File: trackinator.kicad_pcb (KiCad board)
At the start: 2 copper layers, 83 x 33.1 mm, 7 parts, among them U1 ESP32-S3, U2 ESP32-S3, U3 ESP32-S3, U4 ESP32-S3, U5 ESP32-S3, U6 FE2.1

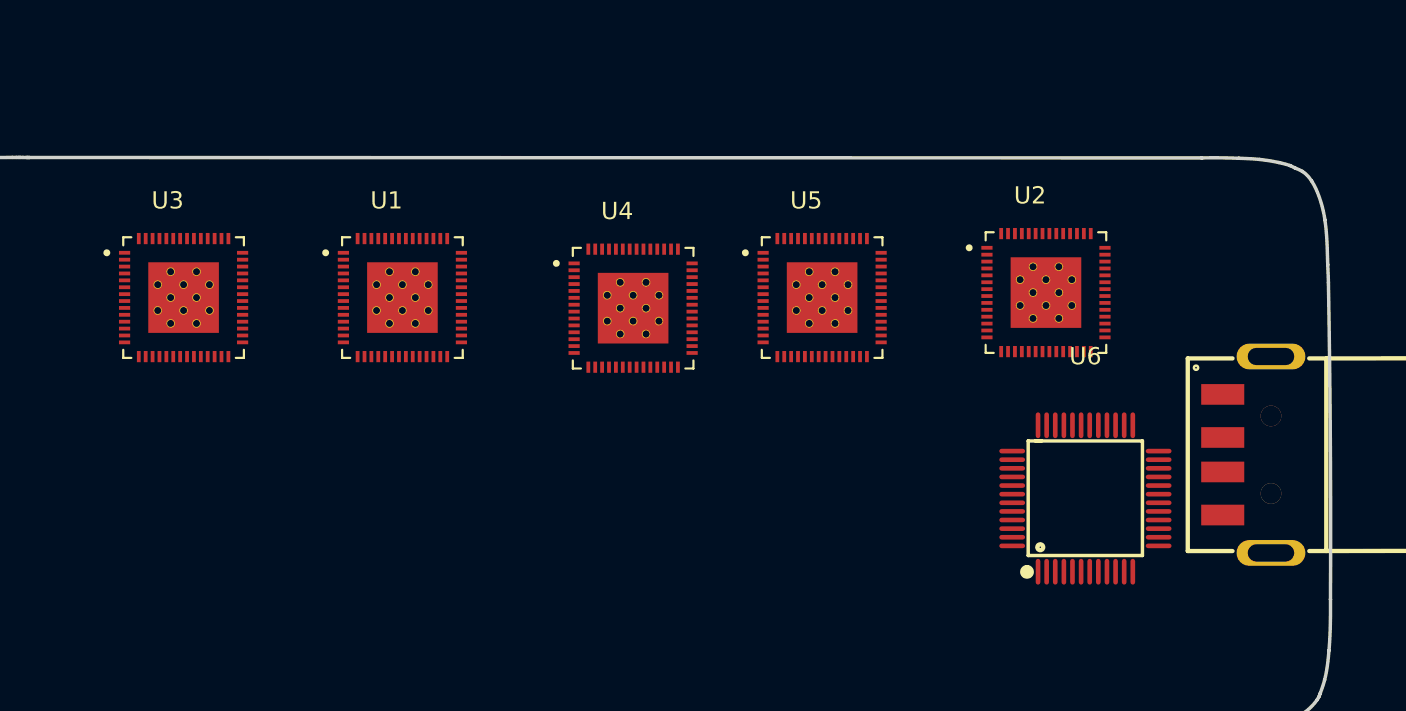
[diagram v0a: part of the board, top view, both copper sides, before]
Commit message: FFC camera connector + pin mapping
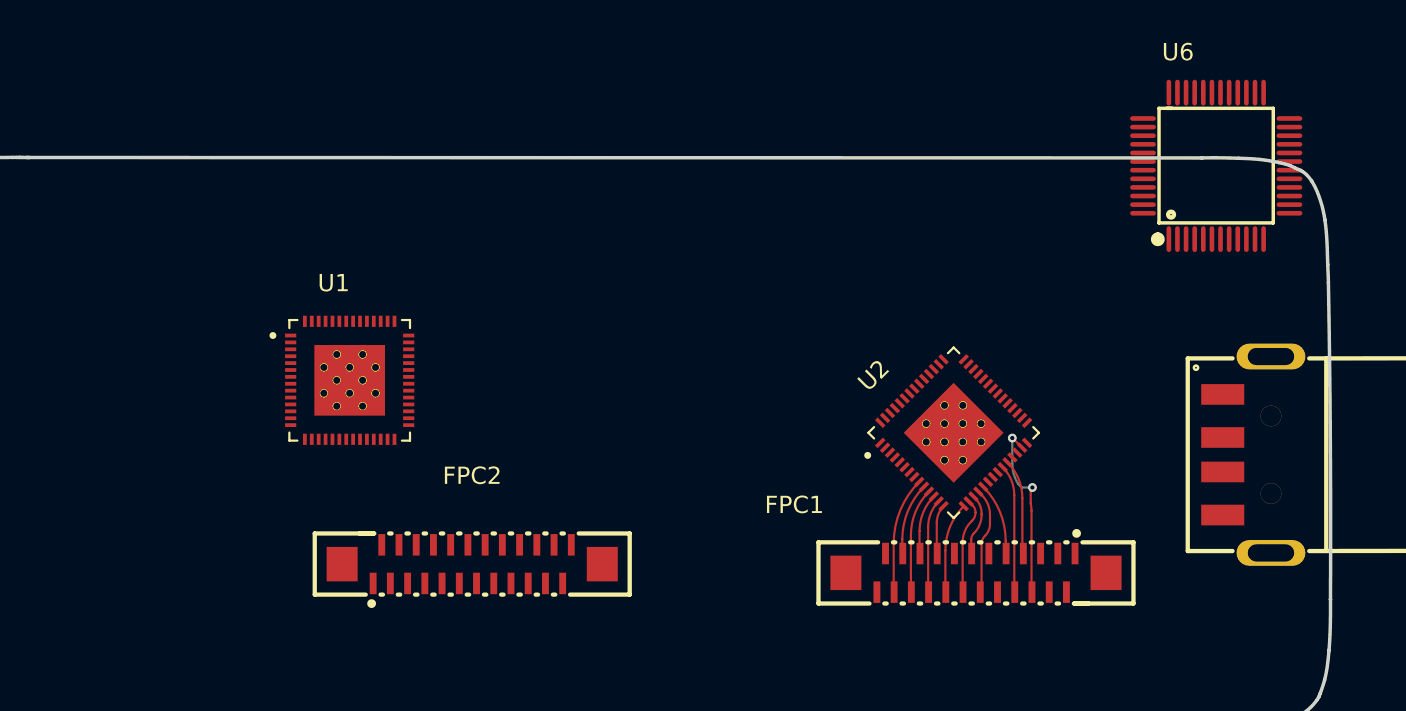
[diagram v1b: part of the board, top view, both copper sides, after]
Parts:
- removed U3, U4, U5: ESP32-S3, mylib:IC_ESP32-S3
- added FPC1: F0503-ZV-24-20T-R, easyeda2kicad:FPC-SMD_F0503-ZV-24-20T-R, F.Cu at (205.3, 57.7)
- added FPC2: F0503-ZV-24-20T-R, easyeda2kicad:FPC-SMD_F0503-ZV-24-20T-R, F.Cu at (176.0, 57.1)
- moved U6 20.7 mm to (219.2, 34.0)
- moved U2 9.74 mm to (204.0, 49.5), turned to 45 degrees
- moved U1 5.69 mm to (168.9, 46.5)
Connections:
- U1 pad 10: unconnected-(U1-GPIO5-Pad10) -> /ESP32_2/DVP_Y3
- U1 pad 11: unconnected-(U1-GPIO6-Pad11) -> /ESP32_2/DVP_Y5
- U1 pad 12: unconnected-(U1-GPIO7-Pad12) -> /ESP32_2/DVP_Y2
- U1 pad 13: unconnected-(U1-GPIO8-Pad13) -> /ESP32_2/DVP_Y6
- U1 pad 14: unconnected-(U1-GPIO9-Pad14) -> /ESP32_2/DVP_PCLK
- U1 pad 15: unconnected-(U1-GPIO10-Pad15) -> /ESP32_2/DVP_Y7
- U1 pad 16: unconnected-(U1-GPIO11-Pad16) -> /ESP32_2/DVP_Y8
- U1 pad 17: unconnected-(U1-GPIO12-Pad17) -> /ESP32_2/XMCLK
- U1 pad 18: unconnected-(U1-GPIO13-Pad18) -> /ESP32_2/DVP_Y9
- U1 pad 19: unconnected-(U1-GPIO14-Pad19) -> /ESP32_2/DVP_HREF
- U1 pad 23: unconnected-(U1-GPIO17-Pad23) -> /ESP32_2/CAM_PWDN
- U1 pad 24: unconnected-(U1-GPIO18-Pad24) -> /ESP32_2/DVP_VSYNC
- U1 pad 25: unconnected-(U1-GPIO19-Pad25) -> /ESP32_2/USB_DN
- U1 pad 26: unconnected-(U1-GPIO20-Pad26) -> /ESP32_2/USB_DP
- U1 pad 27: unconnected-(U1-GPIO21-Pad27) -> /ESP32_2/CAM_RESET
- U1 pad 38: unconnected-(U1-GPIO33-Pad38) -> /ESP32_2/CAM_SCL
- U1 pad 39: unconnected-(U1-GPIO34-Pad39) -> /ESP32_2/CAM_SDA
- U1 pad 9: unconnected-(U1-GPIO4-Pad9) -> /ESP32_2/DVP_Y4
- U2 pad 10: unconnected-(U2-GPIO5-Pad10) -> /ESP32_1/DVP_Y3
- U2 pad 11: unconnected-(U2-GPIO6-Pad11) -> /ESP32_1/DVP_Y5
- U2 pad 12: unconnected-(U2-GPIO7-Pad12) -> /ESP32_1/DVP_Y2
- U2 pad 13: unconnected-(U2-GPIO8-Pad13) -> /ESP32_1/DVP_Y6
- U2 pad 14: unconnected-(U2-GPIO9-Pad14) -> /ESP32_1/DVP_PCLK
- U2 pad 15: unconnected-(U2-GPIO10-Pad15) -> /ESP32_1/DVP_Y7
- U2 pad 16: unconnected-(U2-GPIO11-Pad16) -> /ESP32_1/DVP_Y8
- U2 pad 17: unconnected-(U2-GPIO12-Pad17) -> /ESP32_1/XMCLK
- U2 pad 18: unconnected-(U2-GPIO13-Pad18) -> /ESP32_1/DVP_Y9
- U2 pad 19: unconnected-(U2-GPIO14-Pad19) -> /ESP32_1/DVP_HREF
- U2 pad 23: unconnected-(U2-GPIO17-Pad23) -> /ESP32_1/CAM_PWDN
- U2 pad 24: unconnected-(U2-GPIO18-Pad24) -> /ESP32_1/DVP_VSYNC
- U2 pad 25: unconnected-(U2-GPIO19-Pad25) -> /ESP32_1/USB_DN
- U2 pad 26: unconnected-(U2-GPIO20-Pad26) -> /ESP32_1/USB_DP
- U2 pad 27: unconnected-(U2-GPIO21-Pad27) -> /ESP32_1/CAM_RESET
- U2 pad 38: unconnected-(U2-GPIO33-Pad38) -> /ESP32_1/CAM_SCL
- U2 pad 39: unconnected-(U2-GPIO34-Pad39) -> /ESP32_1/CAM_SDA
- U2 pad 9: unconnected-(U2-GPIO4-Pad9) -> /ESP32_1/DVP_Y4
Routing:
- net /ESP32_1/CAM_RESET: track 0.00 -> 10.6 mm, vias 0 -> 2
- net /ESP32_1/CAM_PWDN: track 0.00 -> 7.43 mm
- net /ESP32_1/DVP_Y4: track 0.00 -> 6.78 mm
- net /ESP32_1/DVP_Y9: track 0.00 -> 6.19 mm
- net /ESP32_1/DVP_Y5: track 0.00 -> 6.11 mm
- net /ESP32_1/DVP_Y8: track 0.00 -> 5.62 mm
- net /ESP32_1/DVP_VSYNC: track 0.00 -> 5.53 mm
- net /ESP32_1/DVP_Y6: track 0.00 -> 5.43 mm
- net /ESP32_1/DVP_Y7: track 0.00 -> 5.26 mm
- net /ESP32_1/DVP_HREF: track 0.00 -> 4.22 mm
- net /ESP32_1/DVP_Y3: track 0.00 -> 4.21 mm
- net /ESP32_1/XMCLK: track 0.00 -> 3.61 mm
- net /ESP32_1/DVP_Y2: track 0.00 -> 3.53 mm
- net /ESP32_1/DVP_PCLK: track 0.00 -> 2.86 mm

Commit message: revving up
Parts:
- removed FPC2: F0503-ZV-24-20T-R, easyeda2kicad:FPC-SMD_F0503-ZV-24-20T-R
- removed U1: ESP32-S3, mylib:IC_ESP32-S3
- moved U6 9.35 mm to (211.7, 39.6), turned to -90 degrees
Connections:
- U6 pad 10: unconnected-(U6-VSS-Pad10) -> GND
- U6 pad 11: unconnected-(U6-DM4-Pad11) -> /ESP32_1/USB_DN
- U6 pad 12: unconnected-(U6-DP4-Pad12) -> /ESP32_1/USB_DP
- U6 pad 21: unconnected-(U6-VD_DLL-Pad21) -> Net-(U6-VD_DLL)
- U6 pad 24: unconnected-(U6-VS_PLL-Pad24) -> GND
- U6 pad 25: unconnected-(U6-VDD18_O-Pad25) -> Net-(U6-VDD18_O)
- U6 pad 27: unconnected-(U6-REXT-Pad27) -> Net-(U6-REXT)
- U6 pad 28: unconnected-(U6-VD18-Pad28) -> Net-(U6-VD_DLL)
- U6 pad 29: unconnected-(U6-DMU-Pad29) -> Net-(U6-DMU)
- U6 pad 30: unconnected-(U6-DPU-Pad30) -> Net-(U6-DPU)
- U6 pad 39: unconnected-(U6-VSS-Pad39) -> GND
- U6 pad 41: unconnected-(U6-VBUSM-Pad41) -> +5V
- U6 pad 6: unconnected-(U6-VD18-Pad6) -> Net-(U6-VD_DLL)
- U6 pad 8: unconnected-(U6-VDD5-Pad8) -> +5V
- U6 pad 9: unconnected-(U6-VD33_O-Pad9) -> Net-(U6-VD33_O)
- USB1 pad 1: unconnected-(USB1-VCC-Pad1) -> +5V
- USB1 pad 2: unconnected-(USB1-D--Pad2) -> Net-(U6-DMU)
- USB1 pad 3: unconnected-(USB1-D+-Pad3) -> Net-(U6-DPU)
- USB1 pad 4: unconnected-(USB1-GND-Pad4) -> GND
- USB1 pad 5: unconnected-(USB1-Pad5) -> GND
- USB1 pad 6: unconnected-(USB1-Pad6) -> GND
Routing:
- net /ESP32_1/CAM_SDA: track 0.00 -> 14.9 mm, vias 0 -> 2
- net /ESP32_1/CAM_SCL: track 0.00 -> 12.9 mm, vias 0 -> 2
- net /ESP32_1/CAM_RESET: track 10.6 -> 8.62 mm, vias 2 -> 0
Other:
- board text added: "> the differential pairs, all of them need to be polarity swapped > scream.wav"

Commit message: grow todo but also do a lot of work
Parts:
- added C1: 10u, Capacitor_SMD:C_0603_1608Metric, F.Cu at (192.3, 16.0)
- added C10: 100n, Capacitor_SMD:C_0402_1005Metric, F.Cu at (205.8, 16.9)
- added C11: 100n, Capacitor_SMD:C_0402_1005Metric, F.Cu at (201.3, 21.3)
- added C12: 100n, Capacitor_SMD:C_0402_1005Metric, F.Cu at (205.0, 8.81)
- added C13: 22u, Capacitor_SMD:C_1206_3216Metric, F.Cu at (234.9, 14.1)
- added C14: 3300p, Capacitor_SMD:C_0402_1005Metric, F.Cu at (232.5, 17.6)
- added C15: 22u, Capacitor_SMD:C_1206_3216Metric, F.Cu at (237.6, 17.6)
- added C16: 100n, Capacitor_SMD:C_0402_1005Metric, F.Cu at (202.8, 43.5)
- added C17: 10u, Capacitor_SMD:C_0603_1608Metric, F.Cu at (162.5, 18.2)
- added C18: 100n, Capacitor_SMD:C_0402_1005Metric, F.Cu at (169.4, -1.27)
- added C19: 10u, Capacitor_SMD:C_0603_1608Metric, F.Cu at (196.8, 45.6)
- added C2: 10u, Capacitor_SMD:C_0603_1608Metric, F.Cu at (204.1, 20.9)
- added C20: 100n, Capacitor_SMD:C_0402_1005Metric, F.Cu at (201.8, 43.5)
- added C21: 100n, Capacitor_SMD:C_0402_1005Metric, F.Cu at (210.1, 51.5)
- added C22: 100n, Capacitor_SMD:C_0402_1005Metric, F.Cu at (200.0, 46.7)
- added C23: 100n, Capacitor_SMD:C_0402_1005Metric, F.Cu at (206.4, 43.6)
- added C24: 100n, Capacitor_SMD:C_0402_1005Metric, F.Cu at (204.4, 53.7)
- added C25: 10u, Capacitor_SMD:C_0603_1608Metric, F.Cu at (196.8, 48.6)
- added C26: 100n, Capacitor_SMD:C_0402_1005Metric, F.Cu at (198.1, 48.3)
- added C27: 10u, Capacitor_SMD:C_0603_1608Metric, F.Cu at (205.6, 56.4)
- added C28: 10u, Capacitor_SMD:C_0603_1608Metric, F.Cu at (212.2, 55.2)
- added C29: 10u, Capacitor_SMD:C_0603_1608Metric, F.Cu at (203.1, 56.4)
- added C3: 100n, Capacitor_SMD:C_0402_1005Metric, F.Cu at (205.6, 15.4)
- added C4: 100n, Capacitor_SMD:C_0402_1005Metric, F.Cu at (205.6, 12.5)
- added C5: 100n, Capacitor_SMD:C_0402_1005Metric, F.Cu at (197.3, 21.7)
- added C6: 100n, Capacitor_SMD:C_0402_1005Metric, F.Cu at (205.6, 18.0)
- added C7: 100n, Capacitor_SMD:C_0402_1005Metric, F.Cu at (199.8, 21.6)
- added C8: 100n, Capacitor_SMD:C_0402_1005Metric, F.Cu at (199.3, 9.09)
- added C9: 100n, Capacitor_SMD:C_0402_1005Metric, F.Cu at (192.8, 17.3)
- added FB1: 100R-800mA, Inductor_SMD:L_0402_1005Metric, F.Cu at (208.7, 55.1)
- added L1: 3n9, Inductor_SMD:L_0402_1005Metric, F.Cu at (198.1, 46.4)
- added LED10: YELLOW, easyeda2kicad:LED0603-RD-YELLOW, F.Cu at (189.1, 1.96)
- added LED11: GREEN, easyeda2kicad:LED0603-RD, F.Cu at (189.2, 3.61)
- added LED12: YELLOW, easyeda2kicad:LED0603-RD-YELLOW, F.Cu at (200.1, -6.05)
- added LED13: GREEN, easyeda2kicad:LED0603-RD, F.Cu at (200.1, -4.39)
- added LED14: YELLOW, easyeda2kicad:LED0603-RD-YELLOW, F.Cu at (223.2, -13.2)
- added LED15: GREEN, easyeda2kicad:LED0603-RD, F.Cu at (223.2, -11.5)
- added LED16: YELLOW, easyeda2kicad:LED0603-RD-YELLOW, F.Cu at (212.0, -14.0)
- added LED17: GREEN, easyeda2kicad:LED0603-RD, F.Cu at (212.0, -12.4)
- added LED3: RED, easyeda2kicad:LED0603-RD, F.Cu at (199.3, 7.08)
- added LED4: YELLOW, easyeda2kicad:LED0603-RD-YELLOW, F.Cu at (181.4, -5.79)
- added LED5: GREEN, easyeda2kicad:LED0603-RD, F.Cu at (181.4, -4.14)
- added LED6: YELLOW, easyeda2kicad:LED0603-RD-YELLOW, F.Cu at (179.8, 1.70)
- added LED7: GREEN, easyeda2kicad:LED0603-RD, F.Cu at (179.9, 3.35)
- added LED8: YELLOW, easyeda2kicad:LED0603-RD-YELLOW, F.Cu at (192.2, -7.32)
- added LED9: GREEN, easyeda2kicad:LED0603-RD, F.Cu at (192.2, -5.66)
- added R1: 4k7, Resistor_SMD:R_0402_1005Metric, F.Cu at (210.7, 43.1)
- added R10: 1k, Resistor_SMD:R_0402_1005Metric, F.Cu at (202.8, 6.91)
- added R12: 1k, Resistor_SMD:R_0402_1005Metric, F.Cu at (184.0, -5.54)
- added R13: 1k, Resistor_SMD:R_0402_1005Metric, F.Cu at (184.0, -4.52)
- added R14: 1k, Resistor_SMD:R_0402_1005Metric, F.Cu at (182.4, 1.96)
- added R15: 1k, Resistor_SMD:R_0402_1005Metric, F.Cu at (182.4, 2.97)
- added R16: 1k, Resistor_SMD:R_0402_1005Metric, F.Cu at (194.8, -7.06)
- added R17: 1k, Resistor_SMD:R_0402_1005Metric, F.Cu at (194.8, -6.05)
- added R18: 1k, Resistor_SMD:R_0402_1005Metric, F.Cu at (191.7, 2.21)
- added R19: 1k, Resistor_SMD:R_0402_1005Metric, F.Cu at (191.7, 3.23)
- added R2: 2k7, Resistor_SMD:R_0402_1005Metric, F.Cu at (208.0, 17.4)
- added R20: 1k, Resistor_SMD:R_0402_1005Metric, F.Cu at (202.6, -5.79)
- added R21: 1k, Resistor_SMD:R_0402_1005Metric, F.Cu at (202.6, -4.78)
- added R22: 1k, Resistor_SMD:R_0402_1005Metric, F.Cu at (225.8, -12.9)
- added R23: 1k, Resistor_SMD:R_0402_1005Metric, F.Cu at (225.8, -11.9)
- added R24: 1k, Resistor_SMD:R_0402_1005Metric, F.Cu at (214.6, -13.8)
- added R25: 1k, Resistor_SMD:R_0402_1005Metric, F.Cu at (214.6, -12.8)
- added R3: 4k7, Resistor_SMD:R_0402_1005Metric, F.Cu at (210.7, 44.1)
- added R4: 10k, Resistor_SMD:R_0402_1005Metric, F.Cu at (202.9, 8.76)
- added R5: 1M21, Resistor_SMD:R_0402_1005Metric, F.Cu at (235.5, 19.0)
- added R6: 383k, Resistor_SMD:R_0402_1005Metric, F.Cu at (233.6, 19.0)
- added R7: 10k, Resistor_SMD:R_0402_1005Metric, F.Cu at (161.9, 20.4)
- added R8: 10k, Resistor_SMD:R_0402_1005Metric, F.Cu at (161.9, 22.4)
- added R9: 1k, Resistor_SMD:R_0402_1005Metric, F.Cu at (205.4, 40.2)
- added SW1: TS-1187A-B-A-B, easyeda2kicad:SW-SMD_4P-L5.1-W5.1-P3.70-LS6.5-TL-2, F.Cu at (155.8, 20.1)
- added SW2: TS-1187A-B-A-B, easyeda2kicad:SW-SMD_4P-L5.1-W5.1-P3.70-LS6.5-TL-2, F.Cu at (155.8, 26.5)
- added U1: M24C02-WMN, Package_SO:SOIC-8_3.9x4.9mm_P1.27mm, F.Cu at (169.8, 4.45)
- added U3: LMZ21701SILR, Snapeda:CONV_TPS82140SILR, F.Cu at (234.7, 16.9)
- added Y1: Crystal_GND24_Small, Crystal:Crystal_SMD_3225-4Pin_3.2x2.5mm, F.Cu at (202.2, 24.9)
- U2: value ESP32-S3 -> ESP32-S3FH4R2; footprint mylib:IC_ESP32-S3 -> mylib:ESP32-S3FH4R2
- moved U6 27.1 mm to (199.1, 15.6)
- moved U2 1.42 mm to (205.1, 48.6), turned to 0 degrees
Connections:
- FPC1 pad 10: VCC_1V8 -> VCC_1V2
- FPC1 pad 4: AVCC_2V8 -> Net-(FPC1-AVDD)
- U2 pad 20: unconnected-(U2-VDD3P3_RTC-Pad20) -> +3V3
- U2 pad 29: unconnected-(U2-VDD_SPI-Pad29) -> Net-(U2-VDD_SPI)
- U2 pad 4: unconnected-(U2-CHIP_PU-Pad4) -> /ESP32_1/CHIP_PU
- U2 pad 44: unconnected-(U2-MTCK-Pad44) -> /ESP32_1/MTCK
- U2 pad 45: unconnected-(U2-MTDO-Pad45) -> /ESP32_1/MTDO
- U2 pad 46: unconnected-(U2-VDD3P3_CPU-Pad46) -> +3V3
- U2 pad 47: unconnected-(U2-MTDI-Pad47) -> /ESP32_1/MTDI
- U2 pad 48: unconnected-(U2-MTMS-Pad48) -> /ESP32_1/MTMS
- U2 pad 49: unconnected-(U2-U0TXD-Pad49) -> Net-(U2-U0TXD)
- U2 pad 5: unconnected-(U2-GPIO0-Pad5) -> /ESP32_1/GPIO0
- U2 pad 55: unconnected-(U2-VDDA1-Pad55) -> +3V3
- U2 pad 56: unconnected-(U2-VDDA2-Pad56) -> +3V3
- U6 pad 1: unconnected-(U6-DRV-Pad1) -> /Config_LED1/DRV
- U6 pad 15: unconnected-(U6-VD33-Pad15) -> +3V3
- U6 pad 2: unconnected-(U6-TESTJ-Pad2) -> /HUB_SDA
- U6 pad 20: unconnected-(U6-VD33-Pad20) -> +3V3
- U6 pad 21: Net-(U6-VD_DLL) -> Net-(U6-VDD18_O)
- U6 pad 22: unconnected-(U6-XIN-Pad22) -> Net-(U6-XIN)
- U6 pad 23: unconnected-(U6-XOUT-Pad23) -> Net-(U6-XOUT)
- U6 pad 26: unconnected-(U6-VD33-Pad26) -> +3V3
- U6 pad 28: Net-(U6-VD_DLL) -> Net-(U6-VDD18_O)
- U6 pad 3: unconnected-(U6-LED[1]-Pad3) -> /HUB_SCL
- U6 pad 31: unconnected-(U6-VD33-Pad31) -> +3V3
- U6 pad 36: unconnected-(U6-VD33-Pad36) -> +3V3
- U6 pad 4: unconnected-(U6-LED[2]-Pad4) -> /Config_LED2/LED
- U6 pad 40: unconnected-(U6-XRSTJ-Pad40) -> Net-(U6-XRSTJ)
- U6 pad 42: unconnected-(U6-VD33-Pad42) -> +3V3
- U6 pad 46: unconnected-(U6-LED[7]-Pad46) -> /Config_LED7/LED
- U6 pad 47: unconnected-(U6-LED[6]-Pad47) -> /Config_LED6/LED
- U6 pad 48: unconnected-(U6-LED[5]-Pad48) -> /Config_LED5/LED
- U6 pad 5: unconnected-(U6-LED[3]-Pad5) -> /Config_LED3/LED
- U6 pad 6: Net-(U6-VD_DLL) -> Net-(U6-VDD18_O)
- U6 pad 7: unconnected-(U6-LED[4]-Pad7) -> /Config_LED4/LED
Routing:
- net /ESP32_1/CAM_SDA: track 14.9 -> 0.00 mm, vias 2 -> 0
- net /ESP32_1/CAM_SCL: track 12.9 -> 0.00 mm, vias 2 -> 0
- net +3V3: track 0.00 -> 9.09 mm, vias 0 -> 2
- net /ESP32_1/CAM_RESET: track 8.62 -> 0.00 mm
- net /ESP32_1/CAM_PWDN: track 7.54 -> 0.00 mm
- net /ESP32_1/DVP_Y4: track 7.08 -> 0.00 mm
- net /ESP32_1/DVP_Y5: track 6.26 -> 0.00 mm
- net /ESP32_1/DVP_Y9: track 6.10 -> 0.00 mm
- net /ESP32_1/DVP_VSYNC: track 5.67 -> 0.00 mm
- net /ESP32_1/DVP_Y8: track 5.58 -> 0.00 mm
- net /ESP32_1/DVP_Y6: track 5.51 -> 0.00 mm
- net /ESP32_1/DVP_Y7: track 5.42 -> 0.00 mm
- net /ESP32_1/DVP_HREF: track 4.43 -> 0.00 mm
- net /ESP32_1/DVP_Y3: track 4.39 -> 0.00 mm
- net /ESP32_1/DVP_Y2: track 3.65 -> 0.00 mm
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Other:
- copper layers 2 -> 4
- board text added: "4 layer is a bit more expensive but has 2X the layers AND smaller traces and vias"
- board text added: "> the differential pairs, all of them have to be polarity swapped > scream.wav"
- board text removed: "> the differential pairs, all of them need to be polarity swapped > scream.wav"

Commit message: crystals and drivers
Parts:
- added C30: 22u, Capacitor_SMD:C_1206_3216Metric, F.Cu at (137.5, 15.2)
- added C31: 3300p, Capacitor_SMD:C_0402_1005Metric, F.Cu at (141.8, 18.5)
- added C32: 22u, Capacitor_SMD:C_1206_3216Metric, F.Cu at (137.5, 18.6)
- added C33: 20p, Capacitor_SMD:C_0402_1005Metric, F.Cu at (201.1, 39.8)
- added C34: 20p, Capacitor_SMD:C_0402_1005Metric, F.Cu at (206.3, 39.7)
- added C35: 100n, Capacitor_SMD:C_0402_1005Metric, F.Cu at (125.7, 41.5)
- added C36: 100n, Capacitor_SMD:C_0402_1005Metric, F.Cu at (123.5, 46.2)
- added C37: 100n, Capacitor_SMD:C_0402_1005Metric, F.Cu at (123.5, 48.1)
- added J1: Conn_01x04_Pin, Connector:FanPinHeader_1x04_P2.54mm_Vertical, F.Cu at (108.8, 72.3)
- added R11: 1M21, Resistor_SMD:R_0402_1005Metric, F.Cu at (141.8, 14.5)
- added R26: 383k, Resistor_SMD:R_0402_1005Metric, F.Cu at (141.8, 16.5)
- added R27: 0, Resistor_SMD:R_0402_1005Metric, F.Cu at (203.2, 42.8)
- added R28: 0, Resistor_SMD:R_0402_1005Metric, F.Cu at (203.7, 43.3)
- added U4: LMZ21701SILR, Snapeda:CONV_TPS82140SILR, F.Cu at (133.0, 16.6)
- added U5: SP3481EN, Package_SO:SOIC-8_3.9x4.9mm_P1.27mm, F.Cu at (125.5, 37.0)
- added U7: SP3481EN, Package_SO:SOIC-8_3.9x4.9mm_P1.27mm, F.Cu at (117.9, 48.4)
- added U8: SP3481EN, Package_SO:SOIC-8_3.9x4.9mm_P1.27mm, F.Cu at (117.9, 54.9)
- added Y2: 40Mhz, Crystal:Crystal_SMD_3225-4Pin_3.2x2.5mm, F.Cu at (203.7, 39.5)
- Y1: value Crystal_GND24_Small -> 12Mhz
- moved R9 7.42 mm to (212.7, 39.0)
- moved C11 2.40 mm to (199.1, 22.1), turned to 90 degrees
- moved Y1 2.23 mm to (201.7, 22.7)
- moved C2 1.96 mm to (205.5, 19.6), turned to 180 degrees
- moved C7 1.74 mm to (198.1, 22.1)
- moved R1 1.22 mm to (211.6, 44.0)
- moved R3 1.22 mm to (211.6, 45.0)
- moved C16 0.58 mm to (202.2, 43.6)
- moved C20 0.53 mm to (201.2, 43.6)
- moved C5 0.18 mm to (197.2, 21.8)
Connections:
- U2 pad 53: unconnected-(U2-XTAL_N-Pad53) -> Net-(U2-XTAL_N)
- U2 pad 54: unconnected-(U2-XTAL_P-Pad54) -> Net-(U2-XTAL_P)
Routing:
- net Net-(U6-XIN): track 0.00 -> 4.43 mm
- net Net-(U6-XOUT): track 0.00 -> 2.73 mm
